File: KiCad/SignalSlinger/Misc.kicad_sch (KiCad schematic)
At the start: 15 parts

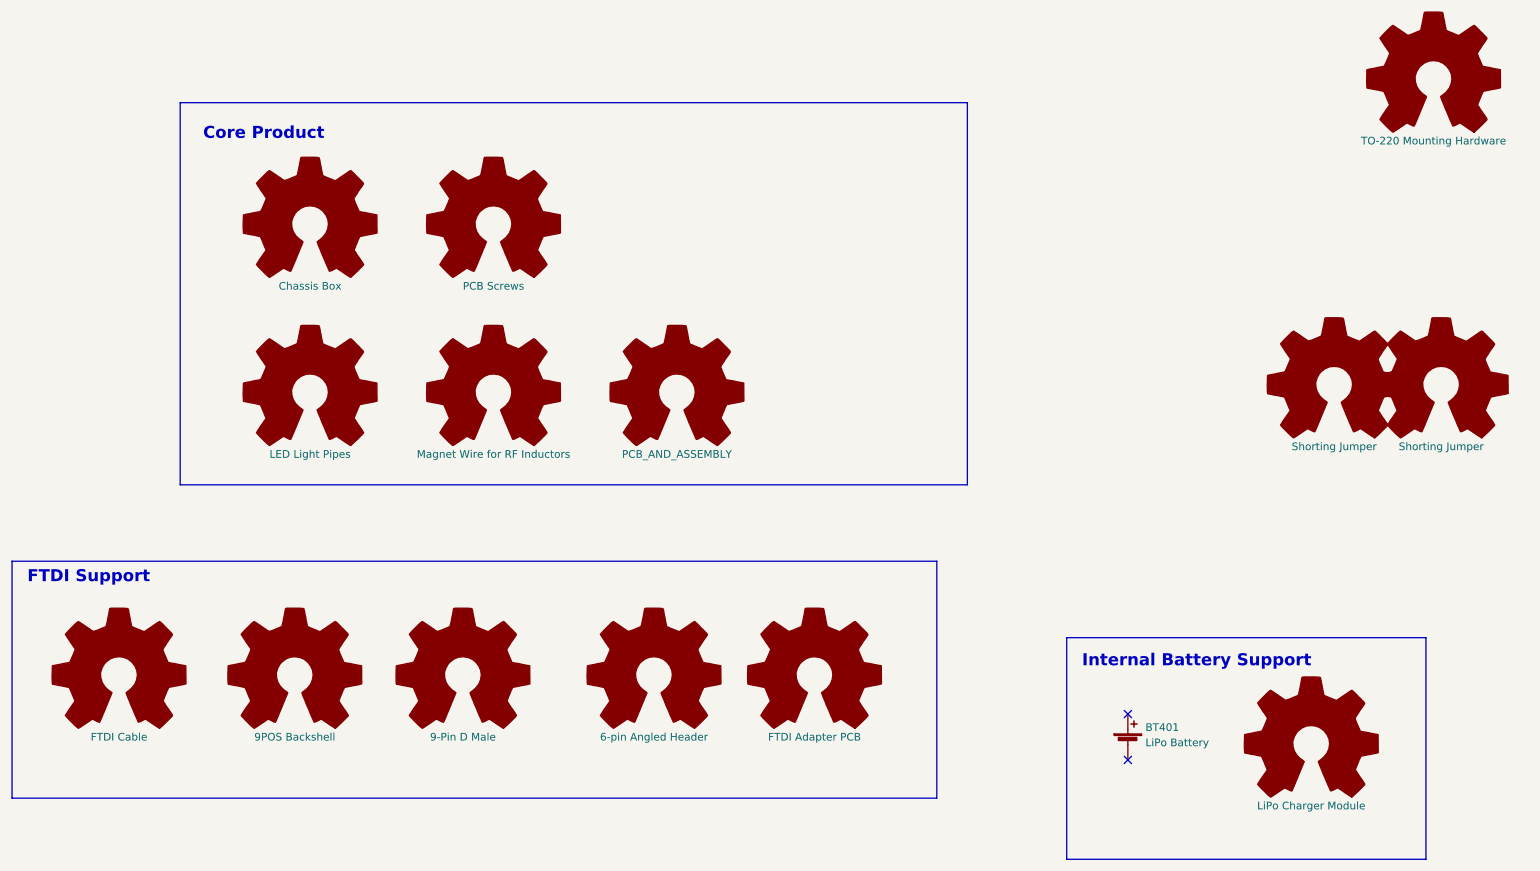
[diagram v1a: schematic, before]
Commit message: Design Updates
oThe boost regulator was removed from the design.
oAn additional load switch was added to the design.
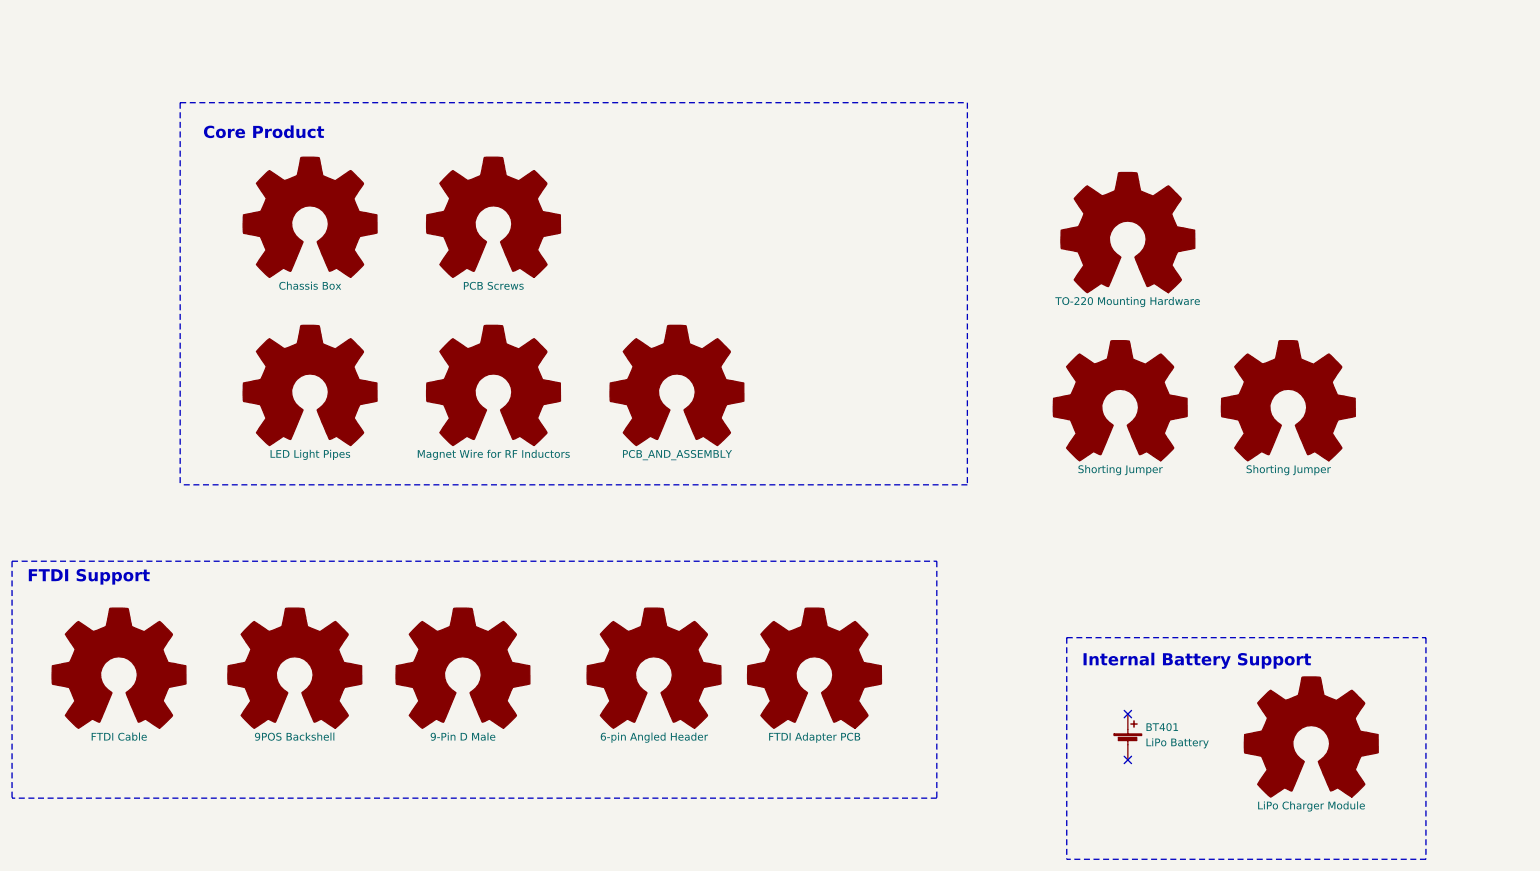
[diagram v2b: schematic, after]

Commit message: Production Updates
Corrects copper spacing issues
Removes warnings
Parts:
- BT401: symbol Device:Battery_Cell -> SignalSlinger Library:Battery_Cell
- HDWR401, HDWR402, HDWR403, HDWR404, HDWR405, HDWR406, HDWR407, HDWR408, HDWR409, HDWR410, HDWR411, HDWR412, HDWR413, HDWR414: symbol Graphic:Logo_Open_Hardware_Large -> SignalSlinger Library:Logo_Open_Hardware_Large
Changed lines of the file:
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@@
 (kicad_sch
-	(version 20231120)
+	(version 20250114)
 	(generator "eeschema")
-	(generator_version "8.0")
+	(generator_version "9.0")
 	(paper "A4")
 	(title_block
@@
 		(date "2024-06-13")
 		(rev "3.4")
-	)
-	(no_connect
-		(at 205.74 147.32)
-	)
-	(no_connect
-		(at 205.74 139.7)
-	)
-	(polyline
-		(pts
-			(xy 48.26 38.1) (xy 48.26 101.6)
-		)
-		(stroke
-			(width 0)
-			(type dash)
-		)
-	)
-	(polyline
-		(pts
-			(xy 255.27 163.83) (xy 195.58 163.83)
-		)
-		(stroke
-			(width 0)
-			(type dash)
-		)
-	)
-	(polyline
-		(pts
-			(xy 179.07 101.6) (xy 48.26 101.6)
-		)
-		(stroke
-			(width 0)
-			(type dash)
-		)
-	)
-	(polyline
-		(pts
-			(xy 173.99 153.67) (xy 20.32 153.67)
-		)
-		(stroke
-			(width 0)
-			(type dash)
-		)
-	)
-	(polyline
-		(pts
-			(xy 48.26 38.1) (xy 179.07 38.1)
-		)
-		(stroke
-			(width 0)
-			(type dash)
-		)
-	)
-	(polyline
-		(pts
-			(xy 20.32 114.3) (xy 20.32 153.67)
-		)
-		(stroke
-			(width 0)
-			(type dash)
-		)
-	)
-	(polyline
-		(pts
-			(xy 255.27 127) (xy 255.27 163.83)
-		)
-		(stroke
-			(width 0)
-			(type dash)
-		)
-	)
-	(polyline
-		(pts
-			(xy 20.32 114.3) (xy 173.99 114.3)
-		)
-		(stroke
-			(width 0)
-			(type dash)
-		)
-	)
-	(polyline
-		(pts
-			(xy 195.58 127) (xy 255.27 127)
-		)
-		(stroke
-			(width 0)
-			(type dash)
-		)
-	)
-	(polyline
-		(pts
-			(xy 179.07 38.1) (xy 179.07 101.6)
-		)
-		(stroke
-			(width 0)
-			(type dash)
-		)
-	)
-	(polyline
-		(pts
-			(xy 173.99 114.3) (xy 173.99 153.67)
-		)
-		(stroke
-			(width 0)
-			(type dash)
-		)
-	)
-	(polyline
-		(pts
-			(xy 195.58 127) (xy 195.58 163.83)
-		)
-		(stroke
-			(width 0)
-			(type dash)
-		)
 	)
 	(text "FTDI Support"
@@
 		)
 	)
-	(symbol
-		(lib_id "Graphic:Logo_Open_Hardware_Large")
+	(no_connect
+		(at 205.74 147.32)
+	)
+	(no_connect
+		(at 205.74 139.7)
+	)
+	(polyline
+		(pts
+			(xy 48.26 38.1) (xy 48.26 101.6)
+		)
+		(stroke
+			(width 0)
+			(type dash)
+		)
+	)
+	(polyline
+		(pts
+			(xy 255.27 163.83) (xy 195.58 163.83)
+		)
+		(stroke
+			(width 0)
+			(type dash)
+		)
+	)
+	(polyline
+		(pts
+			(xy 179.07 101.6) (xy 48.26 101.6)
+		)
+		(stroke
+			(width 0)
+			(type dash)
+		)
+	)
+	(polyline
+		(pts
+			(xy 173.99 153.67) (xy 20.32 153.67)
+		)
+		(stroke
+			(width 0)
+			(type dash)
+		)
+	)
+	(polyline
+		(pts
+			(xy 48.26 38.1) (xy 179.07 38.1)
+		)
+		(stroke
+			(width 0)
+			(type dash)
+		)
+	)
+	(polyline
+		(pts
+			(xy 20.32 114.3) (xy 20.32 153.67)
+		)
+		(stroke
+			(width 0)
+			(type dash)
+		)
+	)
+	(polyline
+		(pts
+			(xy 255.27 127) (xy 255.27 163.83)
+		)
+		(stroke
+			(width 0)
+			(type dash)
+		)
+	)
+	(polyline
+		(pts
+			(xy 20.32 114.3) (xy 173.99 114.3)
+		)
+		(stroke
+			(width 0)
+			(type dash)
+		)
+	)
+	(polyline
+		(pts
+			(xy 195.58 127) (xy 255.27 127)
+		)
+		(stroke
+			(width 0)
+			(type dash)
+		)
+	)
+	(polyline
+		(pts
+			(xy 179.07 38.1) (xy 179.07 101.6)
+		)
+		(stroke
+			(width 0)
+			(type dash)
+		)
+	)
+	(polyline
+		(pts
+			(xy 173.99 114.3) (xy 173.99 153.67)
+		)
+		(stroke
+			(width 0)
+			(type dash)
+		)
+	)
+	(polyline
+		(pts
+			(xy 195.58 127) (xy 195.58 163.83)
+		)
+		(stroke
+			(width 0)
+			(type dash)
+		)
+	)
+	(symbol
+		(lib_id "SignalSlinger Library:Logo_Open_Hardware_Large")
 		(at 127 133.35 0)
 		(unit 1)
@@
 	)
 	(symbol
-		(lib_id "Graphic:Logo_Open_Hardware_Large")
+		(lib_id "SignalSlinger Library:Logo_Open_Hardware_Large")
 		(at 69.85 58.42 0)
 		(unit 1)
@@
 	)
 	(symbol
-		(lib_id "Graphic:Logo_Open_Hardware_Large")
+		(lib_id "SignalSlinger Library:Logo_Open_Hardware_Large")
 		(at 95.25 133.35 0)
 		(unit 1)
@@
 	)
 	(symbol
-		(lib_id "Graphic:Logo_Open_Hardware_Large")
+		(lib_id "SignalSlinger Library:Logo_Open_Hardware_Large")
 		(at 69.85 86.36 0)
 		(unit 1)
@@
 	)
 	(symbol
-		(lib_id "Graphic:Logo_Open_Hardware_Large")
+		(lib_id "SignalSlinger Library:Logo_Open_Hardware_Large")
 		(at 38.1 133.35 0)
 		(unit 1)
@@
 	)
 	(symbol
-		(lib_id "Graphic:Logo_Open_Hardware_Large")
+		(lib_id "SignalSlinger Library:Logo_Open_Hardware_Large")
 		(at 100.33 86.36 0)
 		(unit 1)
@@
 	)
 	(symbol
-		(lib_id "Graphic:Logo_Open_Hardware_Large")
+		(lib_id "SignalSlinger Library:Logo_Open_Hardware_Large")
 		(at 204.47 88.9 0)
 		(unit 1)
@@
 	)
 	(symbol
-		(lib_id "Graphic:Logo_Open_Hardware_Large")
+		(lib_id "SignalSlinger Library:Logo_Open_Hardware_Large")
 		(at 205.74 60.96 0)
 		(unit 1)
@@
 	)
 	(symbol
-		(lib_id "Graphic:Logo_Open_Hardware_Large")
+		(lib_id "SignalSlinger Library:Logo_Open_Hardware_Large")
 		(at 153.67 133.35 0)
 		(unit 1)
@@
 	)
 	(symbol
-		(lib_id "Graphic:Logo_Open_Hardware_Large")
+		(lib_id "SignalSlinger Library:Logo_Open_Hardware_Large")
 		(at 232.41 88.9 0)
 		(unit 1)
@@
 	)
 	(symbol
-		(lib_id "Graphic:Logo_Open_Hardware_Large")
+		(lib_id "SignalSlinger Library:Logo_Open_Hardware_Large")
 		(at 67.31 133.35 0)
 		(unit 1)
@@
 	)
 	(symbol
-		(lib_id "Device:Battery_Cell")
+		(lib_id "SignalSlinger Library:Battery_Cell")
 		(at 205.74 144.78 0)
 		(unit 1)
@@
 	)
 	(symbol
-		(lib_id "Graphic:Logo_Open_Hardware_Large")
+		(lib_id "SignalSlinger Library:Logo_Open_Hardware_Large")
 		(at 130.81 86.36 0)
 		(unit 1)
@@
 	)
 	(symbol
-		(lib_id "Graphic:Logo_Open_Hardware_Large")
+		(lib_id "SignalSlinger Library:Logo_Open_Hardware_Large")
 		(at 100.33 58.42 0)
 		(unit 1)
@@
 	)
 	(symbol
-		(lib_id "Graphic:Logo_Open_Hardware_Large")
+		(lib_id "SignalSlinger Library:Logo_Open_Hardware_Large")
 		(at 236.22 144.78 0)
 		(unit 1)

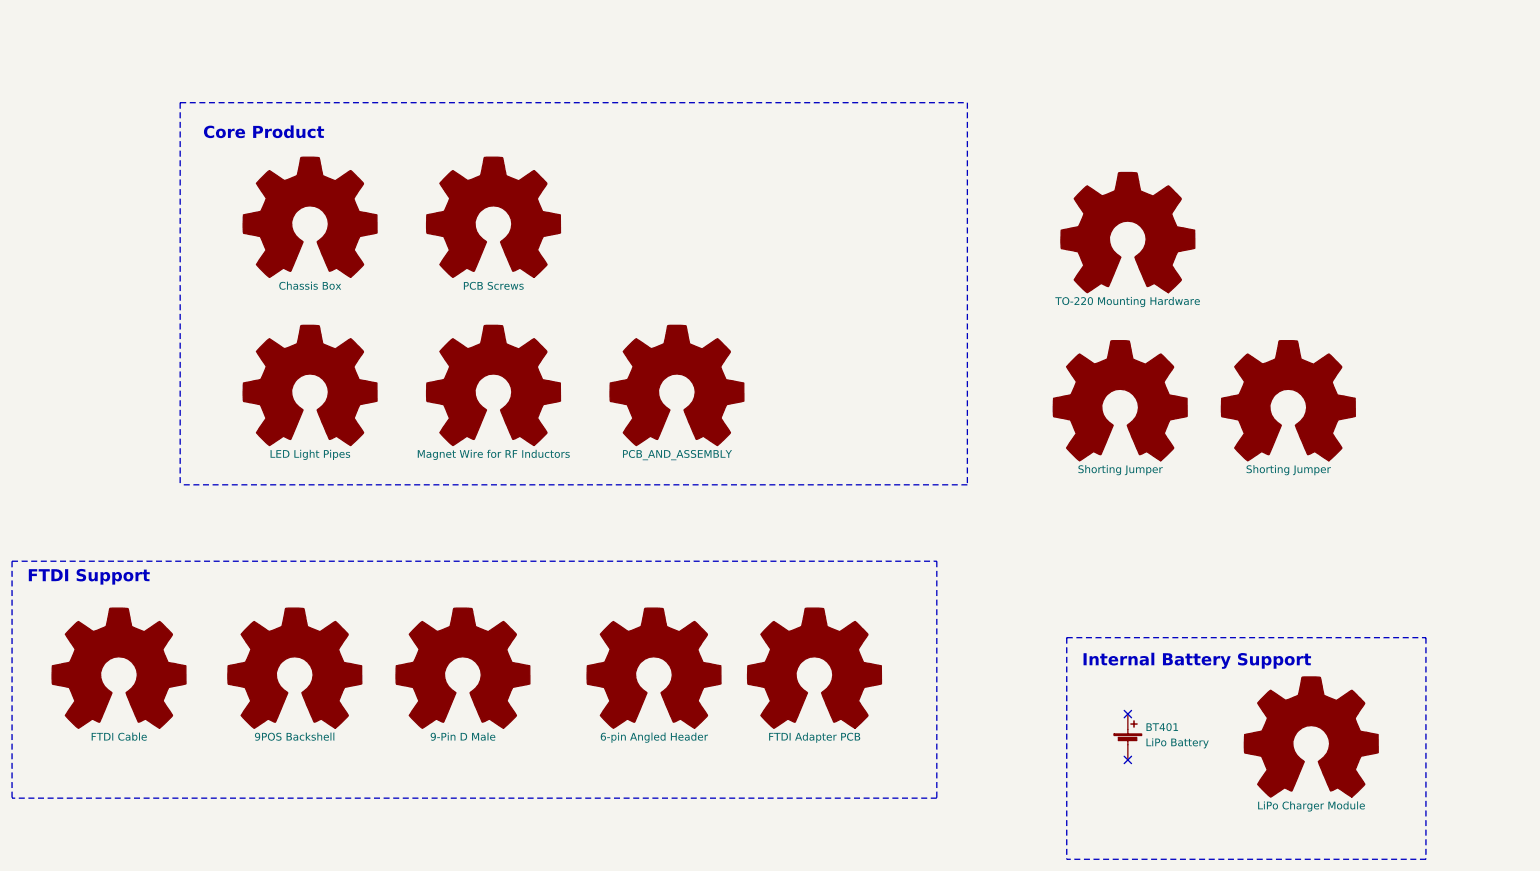
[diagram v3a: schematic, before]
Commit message: Restoring Old KiCad Design
Restoring prototype HW design
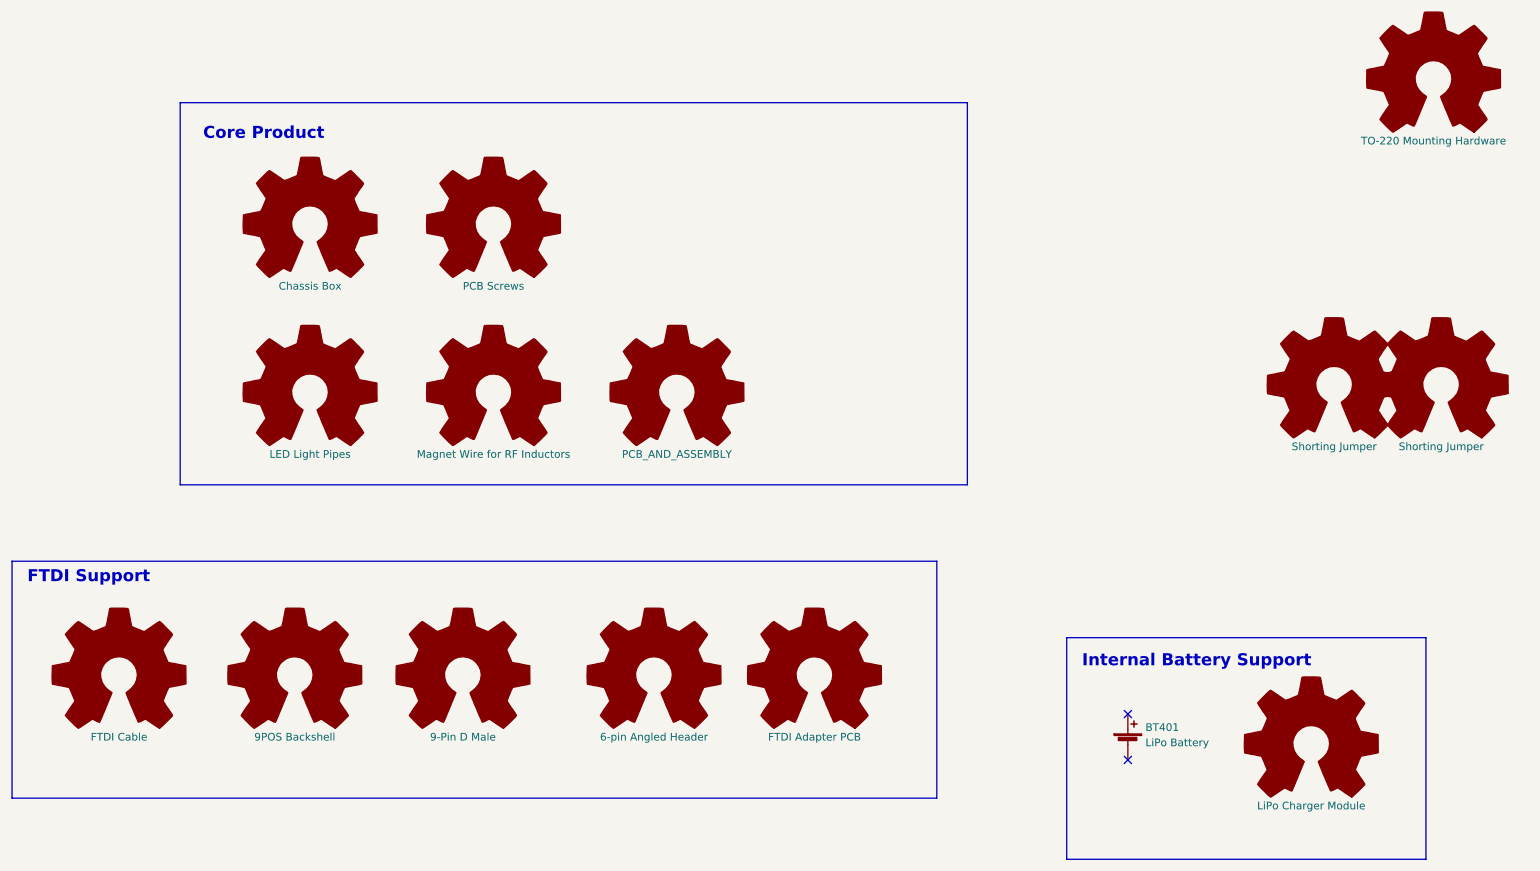
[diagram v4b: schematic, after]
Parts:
- BT401: symbol SignalSlinger Library:Battery_Cell -> Device:Battery_Cell
- HDWR401, HDWR402, HDWR403, HDWR404, HDWR405, HDWR406, HDWR407, HDWR408, HDWR409, HDWR410, HDWR411, HDWR412, HDWR413, HDWR414: symbol SignalSlinger Library:Logo_Open_Hardware_Large -> Graphic:Logo_Open_Hardware_Large

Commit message: Updated to Latest KiCad Version
Updated files
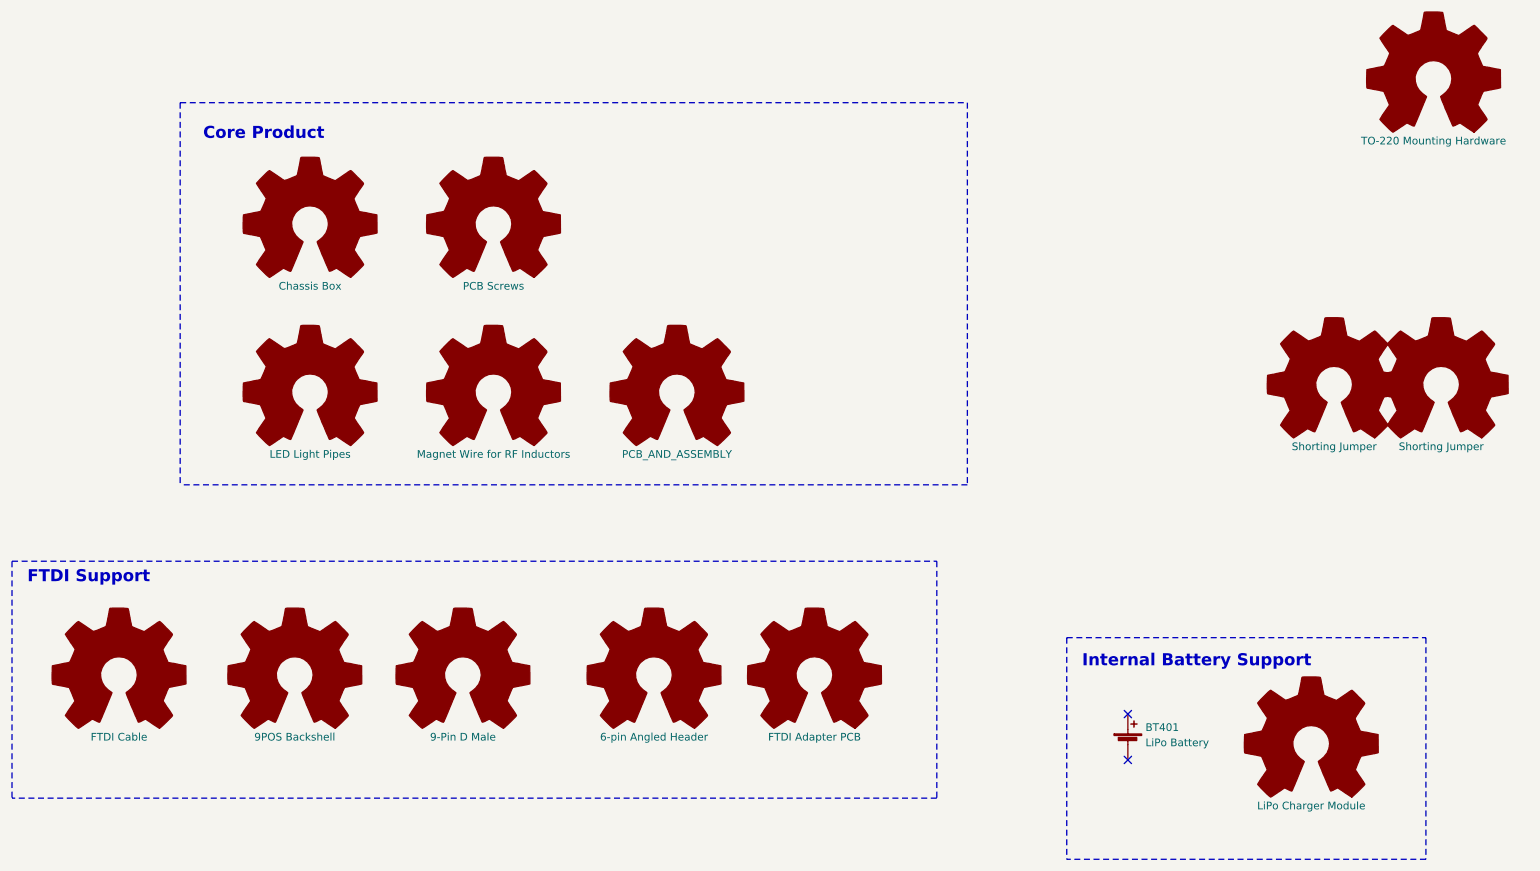
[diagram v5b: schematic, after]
